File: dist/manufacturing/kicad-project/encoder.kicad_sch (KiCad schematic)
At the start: 12 parts, among them J5 B5B-PH-K-S(LF)(SN), U18 AS5047P-ATSM

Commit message: Complete orderable PD1180-EPR board release
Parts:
- removed GND (x3): GND, symbol Custom:rail_down
- removed J5: B5B-PH-K-S(LF)(SN), symbol Device:J_B5B-PH-K-S_LF_SN
- removed V3V3 (x4): V3V3, symbol Custom:rail_up
- added GND (x3): GND, symbol Custom:rail_down
- added TP_ENC_3V3: TP_ENC_3V3, symbol Device:testpoint_right
- added TP_ENC_A: TP_ENC_A, symbol Device:testpoint_right
- added TP_ENC_B: TP_ENC_B, symbol Device:testpoint_right
- added TP_ENC_GND: TP_ENC_GND, symbol Device:testpoint_right
- added TP_ENC_I: TP_ENC_I, symbol Device:testpoint_right
- added V3V3 (x4): V3V3, symbol Custom:rail_up
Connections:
- net at U18.13 (GND), U18.5 (Test): now also GND.1
- net at C52.1, C53.1: now also V3V3.1
- net at C52.2, C53.2: now also GND.1
- net at U18.11 (VDD), U18.12 (VDD3V3): now also V3V3.1
- net at R74.1: now also V3V3.1
- new net: TP_ENC_3V3.1, V3V3.1
- new net: GND.1, TP_ENC_GND.1
- new net ENC_A: TP_ENC_A.1
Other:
- note added: "U18: 14-bit magnetic shaft encoder; SPI readout plus ABI incremental outputs and local 3.3 V filtering."

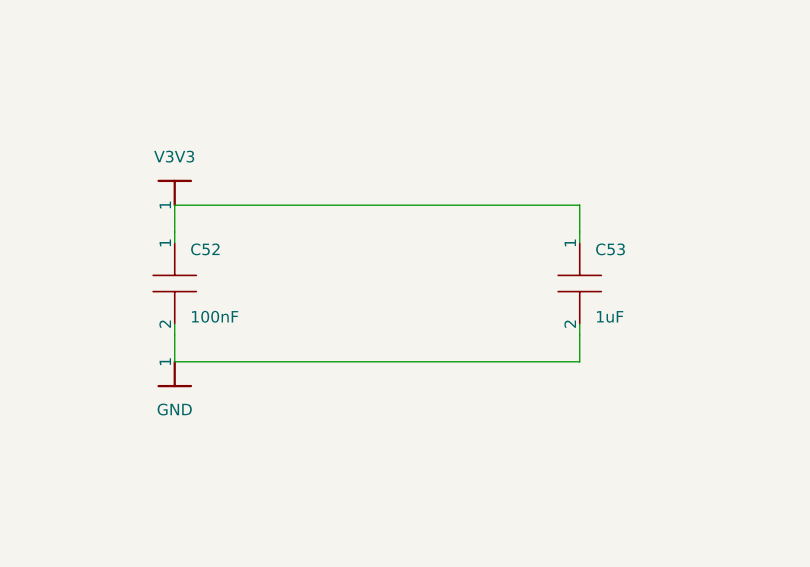
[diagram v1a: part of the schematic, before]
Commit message: Fix schematic style and top-side reset switch
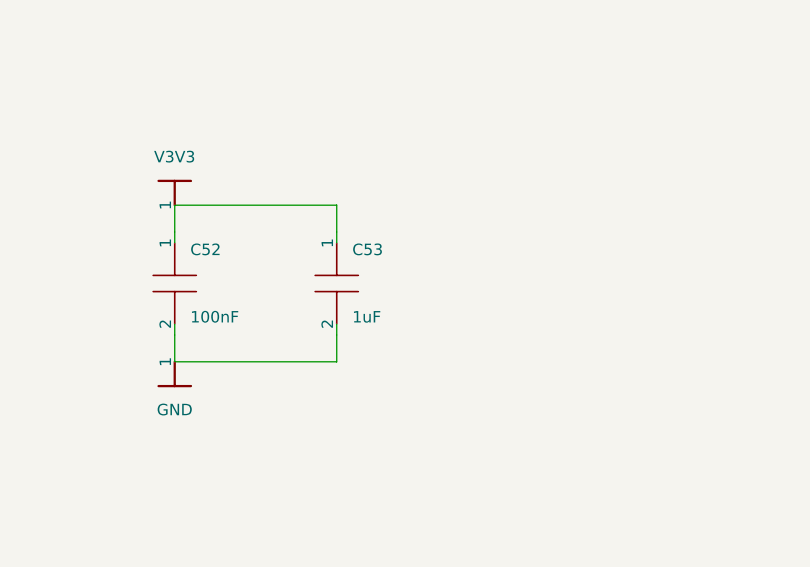
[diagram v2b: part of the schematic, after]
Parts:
- removed GND (x3): GND, symbol Custom:rail_down
- removed V3V3 (x4): V3V3, symbol Custom:rail_up
- added GND (x3): GND, symbol Custom:rail_down
- added V3V3 (x4): V3V3, symbol Custom:rail_up
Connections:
- net at R74.1: now also V3V3.1
- net at TP_ENC_3V3.1: now also V3V3.1
- net at U18.11 (VDD), U18.12 (VDD3V3): now also V3V3.1
- net at TP_ENC_GND.1: now also GND.1
- net at U18.13 (GND), U18.5 (Test): now also GND.1
- net at C52.2, C53.2: now also GND.1
- net at C52.1, C53.1: now also V3V3.1
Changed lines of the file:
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@@
     (instances
       (project ""
-        (path "/f5f6ca0d-0209-4855-99b3-5a1edaa43ca4/760ad9c1-63e8-438c-a628-223798120521"
+        (path "/17a83a49-7a29-40ba-a4d1-006f579ceb16/177ee14c-65ea-43ca-a545-55511f64617c"
           (reference "U18")
           (unit 1)
@@
     (instances
       (project ""
-        (path "/f5f6ca0d-0209-4855-99b3-5a1edaa43ca4/760ad9c1-63e8-438c-a628-223798120521"
+        (path "/17a83a49-7a29-40ba-a4d1-006f579ceb16/177ee14c-65ea-43ca-a545-55511f64617c"
           (reference "R74")
           (unit 1)
@@
     (instances
       (project ""
-        (path "/f5f6ca0d-0209-4855-99b3-5a1edaa43ca4/760ad9c1-63e8-438c-a628-223798120521"
+        (path "/17a83a49-7a29-40ba-a4d1-006f579ceb16/177ee14c-65ea-43ca-a545-55511f64617c"
           (reference "C52")
           (unit 1)
@@
   (symbol
     (lib_id "Device:capacitor_down")
-    (at 290.01375 153.5925 0)
+    (at 263.01375 153.5925 0)
     (unit 1)
     (exclude_from_sim no)
@@
     (property "Reference" "C53"
       (id 0)
-      (at 291.73875 150.5925 0)
+      (at 264.73875 150.5925 0)
       (effects
         (font
@@
     (property "Value" "1uF"
       (id 1)
-      (at 291.73875 156.5925 0)
+      (at 264.73875 156.5925 0)
       (effects
         (font
@@
     (property "Footprint" ""
       (id 2)
-      (at 288.23575 153.5925 90)
-      (effects
-        (font
-          (size 1.27 1.27)
-        )
-        (hide yes)
-      )
-    )
-    (property "Datasheet" "~"
-      (id 3)
-      (at 290.01375 153.5925 0)
+      (at 261.23575 153.5925 90)
+      (effects
+        (font
+          (size 1.27 1.27)
+        )
+        (hide yes)
+      )
+    )
+    (property "Datasheet" "~"
+      (id 3)
+      (at 263.01375 153.5925 0)
       (effects
         (font
@@
     (property "Description" "Capacitor"
       (id 4)
-      (at 290.01375 153.5925 0)
+      (at 263.01375 153.5925 0)
       (effects
         (font
@@
     (instances
       (project ""
-        (path "/f5f6ca0d-0209-4855-99b3-5a1edaa43ca4/760ad9c1-63e8-438c-a628-223798120521"
+        (path "/17a83a49-7a29-40ba-a4d1-006f579ceb16/177ee14c-65ea-43ca-a545-55511f64617c"
           (reference "C53")
           (unit 1)
@@
     (instances
       (project ""
-        (path "/f5f6ca0d-0209-4855-99b3-5a1edaa43ca4/760ad9c1-63e8-438c-a628-223798120521"
+        (path "/17a83a49-7a29-40ba-a4d1-006f579ceb16/177ee14c-65ea-43ca-a545-55511f64617c"
           (reference "TP_ENC_3V3")
           (unit 1)
@@
     (instances
       (project ""
-        (path "/f5f6ca0d-0209-4855-99b3-5a1edaa43ca4/760ad9c1-63e8-438c-a628-223798120521"
+        (path "/17a83a49-7a29-40ba-a4d1-006f579ceb16/177ee14c-65ea-43ca-a545-55511f64617c"
           (reference "TP_ENC_A")
           (unit 1)
@@
     (instances
       (project ""
-        (path "/f5f6ca0d-0209-4855-99b3-5a1edaa43ca4/760ad9c1-63e8-438c-a628-223798120521"
+        (path "/17a83a49-7a29-40ba-a4d1-006f579ceb16/177ee14c-65ea-43ca-a545-55511f64617c"
           (reference "TP_ENC_B")
           (unit 1)
@@
     (instances
       (project ""
-        (path "/f5f6ca0d-0209-4855-99b3-5a1edaa43ca4/760ad9c1-63e8-438c-a628-223798120521"
+        (path "/17a83a49-7a29-40ba-a4d1-006f579ceb16/177ee14c-65ea-43ca-a545-55511f64617c"
           (reference "TP_ENC_I")
           (unit 1)
@@
     (instances
       (project ""
-        (path "/f5f6ca0d-0209-4855-99b3-5a1edaa43ca4/760ad9c1-63e8-438c-a628-223798120521"
+        (path "/17a83a49-7a29-40ba-a4d1-006f579ceb16/177ee14c-65ea-43ca-a545-55511f64617c"
           (reference "TP_ENC_GND")
           (unit 1)
@@
     (instances
       (project ""
-        (path "/f5f6ca0d-0209-4855-99b3-5a1edaa43ca4/760ad9c1-63e8-438c-a628-223798120521"
+        (path "/17a83a49-7a29-40ba-a4d1-006f579ceb16/177ee14c-65ea-43ca-a545-55511f64617c"
           (reference "GND")
           (unit 1)
@@
     (instances
       (project ""
-        (path "/f5f6ca0d-0209-4855-99b3-5a1edaa43ca4/760ad9c1-63e8-438c-a628-223798120521"
+        (path "/17a83a49-7a29-40ba-a4d1-006f579ceb16/177ee14c-65ea-43ca-a545-55511f64617c"
           (reference "GND")
           (unit 1)
@@
     (instances
       (project ""
-        (path "/f5f6ca0d-0209-4855-99b3-5a1edaa43ca4/760ad9c1-63e8-438c-a628-223798120521"
+        (path "/17a83a49-7a29-40ba-a4d1-006f579ceb16/177ee14c-65ea-43ca-a545-55511f64617c"
           (reference "GND")
           (unit 1)
@@
     (instances
       (project ""
-        (path "/f5f6ca0d-0209-4855-99b3-5a1edaa43ca4/760ad9c1-63e8-438c-a628-223798120521"
+        (path "/17a83a49-7a29-40ba-a4d1-006f579ceb16/177ee14c-65ea-43ca-a545-55511f64617c"
           (reference "V3V3")
           (unit 1)
@@
     (instances
       (project ""
-        (path "/f5f6ca0d-0209-4855-99b3-5a1edaa43ca4/760ad9c1-63e8-438c-a628-223798120521"
+        (path "/17a83a49-7a29-40ba-a4d1-006f579ceb16/177ee14c-65ea-43ca-a545-55511f64617c"
           (reference "V3V3")
           (unit 1)
@@
     (instances
       (project ""
-        (path "/f5f6ca0d-0209-4855-99b3-5a1edaa43ca4/760ad9c1-63e8-438c-a628-223798120521"
+        (path "/17a83a49-7a29-40ba-a4d1-006f579ceb16/177ee14c-65ea-43ca-a545-55511f64617c"
           (reference "V3V3")
           (unit 1)
@@
     (instances
       (project ""
-        (path "/f5f6ca0d-0209-4855-99b3-5a1edaa43ca4/760ad9c1-63e8-438c-a628-223798120521"
+        (path "/17a83a49-7a29-40ba-a4d1-006f579ceb16/177ee14c-65ea-43ca-a545-55511f64617c"
           (reference "V3V3")
           (unit 1)
@@
     (pts
       (xy 245.01375000000002 144.89249999999998)
-      (xy 290.01375 144.89249999999998)
+      (xy 263.01375 144.89249999999998)
     )
     (stroke
@@
   (wire
     (pts
-      (xy 290.01375 144.89249999999998)
-      (xy 290.01375 147.89249999999998)
+      (xy 263.01375 144.89249999999998)
+      (xy 263.01375 147.89249999999998)
     )
     (stroke
@@
   (wire
     (pts
-      (xy 290.01375 147.89249999999998)
-      (xy 290.01375 149.0925)
+      (xy 263.01375 147.89249999999998)
+      (xy 263.01375 149.0925)
     )
     (stroke
@@
     (pts
       (xy 245.01375000000002 162.29250000000002)
-      (xy 290.01375 162.29250000000002)
+      (xy 263.01375 162.29250000000002)
     )
     (stroke
@@
   (wire
     (pts
-      (xy 290.01375 162.29250000000002)
-      (xy 290.01375 159.29250000000002)
+      (xy 263.01375 162.29250000000002)
+      (xy 263.01375 159.29250000000002)
     )
     (stroke
@@
   (wire
     (pts
-      (xy 290.01375 159.29250000000002)
-      (xy 290.01375 158.0925)
+      (xy 263.01375 159.29250000000002)
+      (xy 263.01375 158.0925)
     )
     (stroke

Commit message: Use one USB-C port for PD and data
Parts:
- removed GND (x3): GND, symbol Custom:rail_down
- removed V3V3 (x4): V3V3, symbol Custom:rail_up
- added GND (x3): GND, symbol Custom:rail_down
- added V3V3 (x4): V3V3, symbol Custom:rail_up
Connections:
- net at TP_ENC_3V3.1: now also V3V3.1
- net at U18.13 (GND), U18.5 (Test): now also GND.1
- net at TP_ENC_GND.1: now also GND.1
- net at C52.1, C53.1: now also V3V3.1
- net at C52.2, C53.2: now also GND.1
- net at U18.11 (VDD), U18.12 (VDD3V3): now also V3V3.1
- net at R74.1: now also V3V3.1
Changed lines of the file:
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@@
     (instances
       (project ""
-        (path "/17a83a49-7a29-40ba-a4d1-006f579ceb16/177ee14c-65ea-43ca-a545-55511f64617c"
+        (path "/3270f766-a91f-4ae6-bf4b-7f3cb477ac52/15660b54-e8f0-4b56-ae62-dcf2defe2539"
           (reference "U18")
           (unit 1)
@@
     (instances
       (project ""
-        (path "/17a83a49-7a29-40ba-a4d1-006f579ceb16/177ee14c-65ea-43ca-a545-55511f64617c"
+        (path "/3270f766-a91f-4ae6-bf4b-7f3cb477ac52/15660b54-e8f0-4b56-ae62-dcf2defe2539"
           (reference "R74")
           (unit 1)
@@
     (instances
       (project ""
-        (path "/17a83a49-7a29-40ba-a4d1-006f579ceb16/177ee14c-65ea-43ca-a545-55511f64617c"
+        (path "/3270f766-a91f-4ae6-bf4b-7f3cb477ac52/15660b54-e8f0-4b56-ae62-dcf2defe2539"
           (reference "C52")
           (unit 1)
@@
     (instances
       (project ""
-        (path "/17a83a49-7a29-40ba-a4d1-006f579ceb16/177ee14c-65ea-43ca-a545-55511f64617c"
+        (path "/3270f766-a91f-4ae6-bf4b-7f3cb477ac52/15660b54-e8f0-4b56-ae62-dcf2defe2539"
           (reference "C53")
           (unit 1)
@@
     (instances
       (project ""
-        (path "/17a83a49-7a29-40ba-a4d1-006f579ceb16/177ee14c-65ea-43ca-a545-55511f64617c"
+        (path "/3270f766-a91f-4ae6-bf4b-7f3cb477ac52/15660b54-e8f0-4b56-ae62-dcf2defe2539"
           (reference "TP_ENC_3V3")
           (unit 1)
@@
     (instances
       (project ""
-        (path "/17a83a49-7a29-40ba-a4d1-006f579ceb16/177ee14c-65ea-43ca-a545-55511f64617c"
+        (path "/3270f766-a91f-4ae6-bf4b-7f3cb477ac52/15660b54-e8f0-4b56-ae62-dcf2defe2539"
           (reference "TP_ENC_A")
           (unit 1)
@@
     (instances
       (project ""
-        (path "/17a83a49-7a29-40ba-a4d1-006f579ceb16/177ee14c-65ea-43ca-a545-55511f64617c"
+        (path "/3270f766-a91f-4ae6-bf4b-7f3cb477ac52/15660b54-e8f0-4b56-ae62-dcf2defe2539"
           (reference "TP_ENC_B")
           (unit 1)
@@
     (instances
       (project ""
-        (path "/17a83a49-7a29-40ba-a4d1-006f579ceb16/177ee14c-65ea-43ca-a545-55511f64617c"
+        (path "/3270f766-a91f-4ae6-bf4b-7f3cb477ac52/15660b54-e8f0-4b56-ae62-dcf2defe2539"
           (reference "TP_ENC_I")
           (unit 1)
@@
     (instances
       (project ""
-        (path "/17a83a49-7a29-40ba-a4d1-006f579ceb16/177ee14c-65ea-43ca-a545-55511f64617c"
+        (path "/3270f766-a91f-4ae6-bf4b-7f3cb477ac52/15660b54-e8f0-4b56-ae62-dcf2defe2539"
           (reference "TP_ENC_GND")
           (unit 1)
@@
     (instances
       (project ""
-        (path "/17a83a49-7a29-40ba-a4d1-006f579ceb16/177ee14c-65ea-43ca-a545-55511f64617c"
+        (path "/3270f766-a91f-4ae6-bf4b-7f3cb477ac52/15660b54-e8f0-4b56-ae62-dcf2defe2539"
           (reference "GND")
           (unit 1)
@@
     (instances
       (project ""
-        (path "/17a83a49-7a29-40ba-a4d1-006f579ceb16/177ee14c-65ea-43ca-a545-55511f64617c"
+        (path "/3270f766-a91f-4ae6-bf4b-7f3cb477ac52/15660b54-e8f0-4b56-ae62-dcf2defe2539"
           (reference "GND")
           (unit 1)
@@
     (instances
       (project ""
-        (path "/17a83a49-7a29-40ba-a4d1-006f579ceb16/177ee14c-65ea-43ca-a545-55511f64617c"
+        (path "/3270f766-a91f-4ae6-bf4b-7f3cb477ac52/15660b54-e8f0-4b56-ae62-dcf2defe2539"
           (reference "GND")
           (unit 1)
@@
     (instances
       (project ""
-        (path "/17a83a49-7a29-40ba-a4d1-006f579ceb16/177ee14c-65ea-43ca-a545-55511f64617c"
+        (path "/3270f766-a91f-4ae6-bf4b-7f3cb477ac52/15660b54-e8f0-4b56-ae62-dcf2defe2539"
           (reference "V3V3")
           (unit 1)
@@
     (instances
       (project ""
-        (path "/17a83a49-7a29-40ba-a4d1-006f579ceb16/177ee14c-65ea-43ca-a545-55511f64617c"
+        (path "/3270f766-a91f-4ae6-bf4b-7f3cb477ac52/15660b54-e8f0-4b56-ae62-dcf2defe2539"
           (reference "V3V3")
           (unit 1)
@@
     (instances
       (project ""
-        (path "/17a83a49-7a29-40ba-a4d1-006f579ceb16/177ee14c-65ea-43ca-a545-55511f64617c"
+        (path "/3270f766-a91f-4ae6-bf4b-7f3cb477ac52/15660b54-e8f0-4b56-ae62-dcf2defe2539"
           (reference "V3V3")
           (unit 1)
@@
     (instances
       (project ""
-        (path "/17a83a49-7a29-40ba-a4d1-006f579ceb16/177ee14c-65ea-43ca-a545-55511f64617c"
+        (path "/3270f766-a91f-4ae6-bf4b-7f3cb477ac52/15660b54-e8f0-4b56-ae62-dcf2defe2539"
           (reference "V3V3")
           (unit 1)

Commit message: fix: finalize single-port EPR controller
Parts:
- removed GND (x3): GND, symbol Custom:rail_down
- removed V3V3 (x4): V3V3, symbol Custom:rail_up
- C52, C53: footprint (none) -> capacitor_cap0603
- R74: footprint (none) -> resistor_res0603
- TP_ENC_3V3, TP_ENC_A, TP_ENC_B, TP_ENC_GND, TP_ENC_I: footprint (none) -> test_point
- U18: footprint (none) -> AS5047P-ATSM
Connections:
- net ENC_A: now also U18.7 (A)
- net V3V3: now reaches C52.1, C53.1
- net V3V3: now also R74.1, TP_ENC_3V3.1, U18.11 (VDD), U18.12 (VDD3V3)
- net GND: now reaches C52.2, C53.2
- net GND: now also TP_ENC_GND.1, U18.13 (GND), U18.5 (Test)
- net ENC_CS_N: now reaches R74.2
- net ENC_CS_N: now also U18.1 (CSn)
- net ENC_B: now reaches TP_ENC_B.1
- net ENC_B: now also U18.6 (B)
- net ENC_I: now reaches U18.14 (I)
- net ENC_I: now also TP_ENC_I.1
- net SPI_SCK: now reaches U18.2 (CLK)
- net SPI_MISO: now reaches U18.3 (MISO)
- net SPI_MOSI: now reaches U18.4 (MOSI)
- no-connect marks 0 -> 3
